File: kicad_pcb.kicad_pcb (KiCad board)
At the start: 2 copper layers, 285 x 95.1 mm, 163 parts, among them J1 USB_B_Mini, SW1 SW_Push, U1 ATmega32U4-AU, Y1 Resonator_Small

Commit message: rerouted the bottom row
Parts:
- added D23: D_Small, Diode_SMD:D_0805_2012Metric, B.Cu at (293.8, 120.0)
- added D38: D_Small, Diode_SMD:D_0805_2012Metric, B.Cu at (310.4, 120.0)
- added D66: D_Small, Diode_SMD:D_0805_2012Metric, B.Cu at (291.3, 120.0)
- added D69: D_Small, Diode_SMD:D_0805_2012Metric, B.Cu at (330.2, 120.0)
- added MX23: R ALT, MX_Alps_Hybrid:MX-2U-NoLED, F.Cu at (287.3, 125.4)
- added MX38: R WIN, MX_Alps_Hybrid:MX-1.25U-NoLED, F.Cu at (294.5, 125.4)
- added MX62-1: CTRL, MX_Alps_Hybrid:MX-1.5U-NoLED, F.Cu at (77.8, 125.4)
- added MX63-1: WIN, MX_Alps_Hybrid:MX-1.25U-NoLED, F.Cu at (104.0, 125.4)
- added MX64-1: ALT, MX_Alps_Hybrid:MX-1.5U-NoLED, F.Cu at (130.2, 125.4)
- added MX65-1: L SPACE, MX_Alps_Hybrid:MX-2.75U-ReversedStabilizers-NoLED, F.Cu at (170.7, 125.4)
- added MX66: R ALT, MX_Alps_Hybrid:MX-1.5U-NoLED, F.Cu at (268.3, 125.4)
- added MX69: R CTRL, MX_Alps_Hybrid:MX-2.25U-NoLED, F.Cu at (327.8, 125.4)
- added MX70-1: R SPACE, MX_Alps_Hybrid:MX-2.75U-NoLED, F.Cu at (242.1, 125.4)
- MX61: footprint MX_Alps_Hybrid:MXOnly-1U-NoLED -> MX_Alps_Hybrid:MX-1U-NoLED
- MX62, MX63, MX64: footprint MX_Alps_Hybrid:MXOnly-1.25U-NoLED -> MX_Alps_Hybrid:MX-1.25U-NoLED
- MX65: value LEFT SPACE -> L SPACE; footprint MX_Alps_Hybrid:MXOnly-2.25U-ReversedStabilizers-NoLED -> MX_Alps_Hybrid:MX-2.25U-ReversedStabilizers-NoLED
- MX70: value RIGHT SPACE -> R SPACE
- moved D70 26.7 mm to (262.7, 119.9), turned to 270 degrees
- moved D75 14.0 mm to (333.4, 120.0), turned to 270 degrees
- moved D71 10.9 mm to (269.9, 119.9), turned to 270 degrees
- moved D72 10.8 mm to (288.9, 120.0), turned to 270 degrees
- moved D74 10.8 mm to (327.0, 120.0), turned to 270 degrees
- moved D73 10.7 mm to (307.6, 120.0), turned to 270 degrees
- moved D61 4.62 mm to (81.0, 130.3)
- turned MX61 to 180 degrees
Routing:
- net COL7: track 82.1 -> 214.2 mm, vias 1 -> 2
- net COL8: track 90.6 -> 219.8 mm, vias 2 -> 4
- net COL5: track 93.4 -> 219.9 mm, vias 1 -> 3
- net ROW1: track 296.0 -> 352.8 mm, vias 4 -> 6
- net Net-(D66-Pad2): track 0.00 -> 34.6 mm
- net Net-(D23-Pad2): track 0.00 -> 34.2 mm
- net ROW2: track 286.1 -> 313.0 mm, vias 2 -> 4
- net Net-(D70-Pad2): track 9.31 -> 35.9 mm
- net Net-(D38-Pad2): track 0.00 -> 18.8 mm
- net Net-(D62-Pad2): track 9.31 -> 27.1 mm
- net COL9: track 133.1 -> 150.8 mm
- net COL1: track 189.1 -> 205.3 mm
- net Net-(D63-Pad2): track 9.31 -> 24.9 mm
- net Net-(D65-Pad2): track 9.31 -> 23.8 mm
- net Net-(D64-Pad2): track 9.37 -> 23.1 mm
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
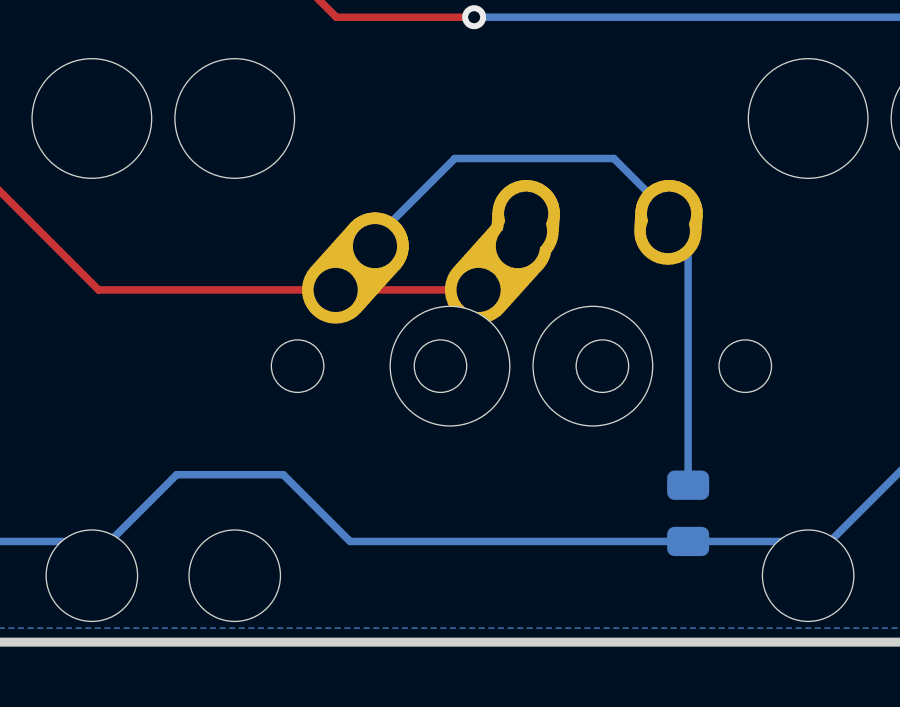
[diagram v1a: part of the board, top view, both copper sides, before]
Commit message: tidied up some overlapping pads
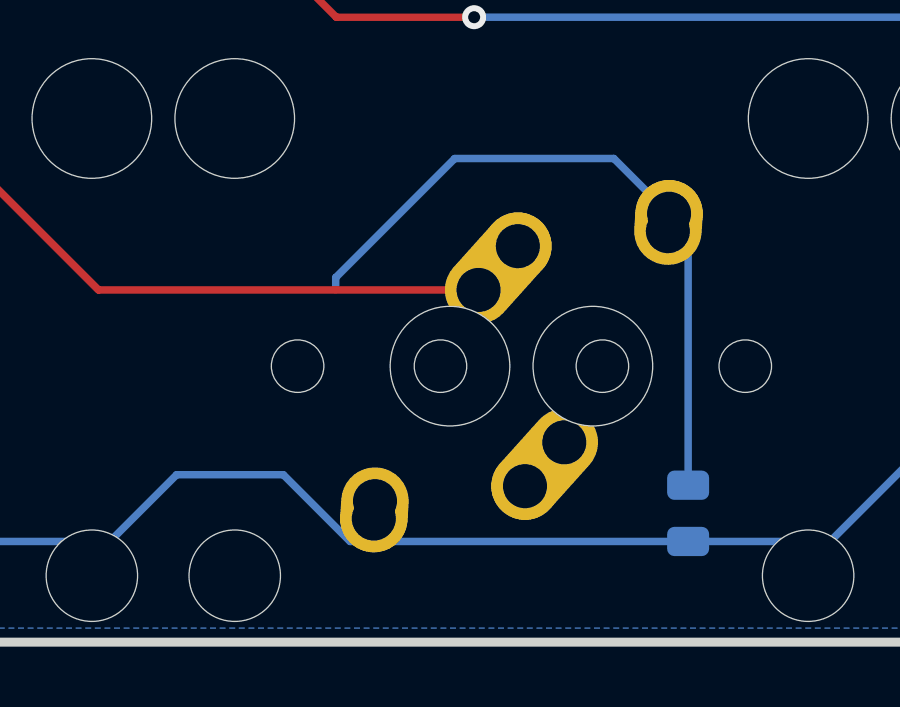
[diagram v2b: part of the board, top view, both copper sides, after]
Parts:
- MX65: value L SPACE -> L SPACE (2.25u)
- MX65-1: value L SPACE -> L SPACE (2.75u); footprint MX_Alps_Hybrid:MX-2.75U-ReversedStabilizers-NoLED -> MX_Alps_Hybrid:MX-2.75U-NoLED
- turned MX65-1 to 180 degrees
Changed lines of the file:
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@@
       (effects (font (size 1 1) (thickness 0.15)))
     )
-    (fp_text value "L SPACE" (at 0 -7.9375) (layer Dwgs.User)
+    (fp_text value "L SPACE (2.25u)" (at -2.38125 -7.9375) (layer Dwgs.User)
       (effects (font (size 1 1) (thickness 0.15)))
     )
@@
     (pad 2 thru_hole oval (at 2.5 -4.5 86.0548) (size 2.831378 2.25) (drill 1.47 (offset 0.290689 0)) (layers *.Cu B.Mask)
       (net 87 "Net-(D64-Pad2)"))
-  )
-  (module MX_Alps_Hybrid:MX-2.75U-ReversedStabilizers-NoLED (layer F.Cu)
-    (at 170.65625 125.4125)
-    (fp_text reference MX65-1 (at 0 3.175) (layer Dwgs.User)
-      (effects (font (size 1 1) (thickness 0.15)))
-    )
-    (fp_text value "L SPACE" (at 0 -7.9375) (layer Dwgs.User)
-      (effects (font (size 1 1) (thickness 0.15)))
-    )
-    (fp_line (start 5 -7) (end 7 -7) (layer Dwgs.User) (width 0.15))
-    (fp_line (start 7 -7) (end 7 -5) (layer Dwgs.User) (width 0.15))
-    (fp_line (start 5 7) (end 7 7) (layer Dwgs.User) (width 0.15))
-    (fp_line (start 7 7) (end 7 5) (layer Dwgs.User) (width 0.15))
-    (fp_line (start -7 5) (end -7 7) (layer Dwgs.User) (width 0.15))
-    (fp_line (start -7 7) (end -5 7) (layer Dwgs.User) (width 0.15))
-    (fp_line (start -5 -7) (end -7 -7) (layer Dwgs.User) (width 0.15))
-    (fp_line (start -7 -7) (end -7 -5) (layer Dwgs.User) (width 0.15))
-    (fp_line (start -26.19375 -9.525) (end 26.19375 -9.525) (layer Dwgs.User) (width 0.15))
-    (fp_line (start 26.19375 -9.525) (end 26.19375 9.525) (layer Dwgs.User) (width 0.15))
-    (fp_line (start -26.19375 9.525) (end 26.19375 9.525) (layer Dwgs.User) (width 0.15))
-    (fp_line (start -26.19375 9.525) (end -26.19375 -9.525) (layer Dwgs.User) (width 0.15))
-    (pad 2 thru_hole oval (at 2.5 -4.5 86.0548) (size 2.831378 2.25) (drill 1.47 (offset 0.290689 0)) (layers *.Cu B.Mask)
-      (net 22 COL4))
-    (pad 2 thru_hole circle (at 2.54 -5.08) (size 2.25 2.25) (drill 1.47) (layers *.Cu B.Mask)
-      (net 22 COL4))
-    (pad 1 thru_hole oval (at -3.81 -2.54 48.0996) (size 4.211556 2.25) (drill 1.47 (offset 0.980778 0)) (layers *.Cu B.Mask)
-      (net 88 "Net-(D65-Pad2)"))
-    (pad "" np_thru_hole circle (at 0 0) (size 3.9878 3.9878) (drill 3.9878) (layers *.Cu *.Mask))
-    (pad 1 thru_hole circle (at -2.5 -4) (size 2.25 2.25) (drill 1.47) (layers *.Cu B.Mask)
-      (net 88 "Net-(D65-Pad2)"))
-    (pad "" np_thru_hole circle (at -5.08 0 48.0996) (size 1.75 1.75) (drill 1.75) (layers *.Cu *.Mask))
-    (pad "" np_thru_hole circle (at 5.08 0 48.0996) (size 1.75 1.75) (drill 1.75) (layers *.Cu *.Mask))
-    (pad "" np_thru_hole circle (at -11.938 6.985) (size 3.048 3.048) (drill 3.048) (layers *.Cu *.Mask))
-    (pad "" np_thru_hole circle (at 11.938 6.985) (size 3.048 3.048) (drill 3.048) (layers *.Cu *.Mask))
-    (pad "" np_thru_hole circle (at -11.938 -8.255) (size 3.9878 3.9878) (drill 3.9878) (layers *.Cu *.Mask))
-    (pad "" np_thru_hole circle (at 11.938 -8.255) (size 3.9878 3.9878) (drill 3.9878) (layers *.Cu *.Mask))
   )
   (module Diode_SMD:D_0805_2012Metric (layer B.Cu)
@@
     )
   )
+  (module MX_Alps_Hybrid:MX-2.75U-NoLED (layer F.Cu)
+    (at 170.65625 125.4125 180)
+    (fp_text reference MX65-1 (at 0 3.175) (layer Dwgs.User)
+      (effects (font (size 1 1) (thickness 0.15)))
+    )
+    (fp_text value "L SPACE (2.75u)" (at -2.38125 -7.9375) (layer Dwgs.User)
+      (effects (font (size 1 1) (thickness 0.15)))
+    )
+    (fp_line (start 5 -7) (end 7 -7) (layer Dwgs.User) (width 0.15))
+    (fp_line (start 7 -7) (end 7 -5) (layer Dwgs.User) (width 0.15))
+    (fp_line (start 5 7) (end 7 7) (layer Dwgs.User) (width 0.15))
+    (fp_line (start 7 7) (end 7 5) (layer Dwgs.User) (width 0.15))
+    (fp_line (start -7 5) (end -7 7) (layer Dwgs.User) (width 0.15))
+    (fp_line (start -7 7) (end -5 7) (layer Dwgs.User) (width 0.15))
+    (fp_line (start -5 -7) (end -7 -7) (layer Dwgs.User) (width 0.15))
+    (fp_line (start -7 -7) (end -7 -5) (layer Dwgs.User) (width 0.15))
+    (fp_line (start -26.19375 -9.525) (end 26.19375 -9.525) (layer Dwgs.User) (width 0.15))
+    (fp_line (start 26.19375 -9.525) (end 26.19375 9.525) (layer Dwgs.User) (width 0.15))
+    (fp_line (start -26.19375 9.525) (end 26.19375 9.525) (layer Dwgs.User) (width 0.15))
+    (fp_line (start -26.19375 9.525) (end -26.19375 -9.525) (layer Dwgs.User) (width 0.15))
+    (pad 2 thru_hole oval (at 2.5 -4.5 266.0548) (size 2.831378 2.25) (drill 1.47 (offset 0.290689 0)) (layers *.Cu B.Mask)
+      (net 22 COL4))
+    (pad 2 thru_hole circle (at 2.54 -5.08 180) (size 2.25 2.25) (drill 1.47) (layers *.Cu B.Mask)
+      (net 22 COL4))
+    (pad 1 thru_hole oval (at -3.81 -2.54 228.0996) (size 4.211556 2.25) (drill 1.47 (offset 0.980778 0)) (layers *.Cu B.Mask)
+      (net 88 "Net-(D65-Pad2)"))
+    (pad "" np_thru_hole circle (at 0 0 180) (size 3.9878 3.9878) (drill 3.9878) (layers *.Cu *.Mask))
+    (pad 1 thru_hole circle (at -2.5 -4 180) (size 2.25 2.25) (drill 1.47) (layers *.Cu B.Mask)
+      (net 88 "Net-(D65-Pad2)"))
+    (pad "" np_thru_hole circle (at -5.08 0 228.0996) (size 1.75 1.75) (drill 1.75) (layers *.Cu *.Mask))
+    (pad "" np_thru_hole circle (at 5.08 0 228.0996) (size 1.75 1.75) (drill 1.75) (layers *.Cu *.Mask))
+    (pad "" np_thru_hole circle (at -11.938 -6.985 180) (size 3.048 3.048) (drill 3.048) (layers *.Cu *.Mask))
+    (pad "" np_thru_hole circle (at 11.938 -6.985 180) (size 3.048 3.048) (drill 3.048) (layers *.Cu *.Mask))
+    (pad "" np_thru_hole circle (at -11.938 8.255 180) (size 3.9878 3.9878) (drill 3.9878) (layers *.Cu *.Mask))
+    (pad "" np_thru_hole circle (at 11.938 8.255 180) (size 3.9878 3.9878) (drill 3.9878) (layers *.Cu *.Mask))
+  )
   (gr_text "Katana60 revision 2\nby RominRonin in association with CandyKeys.com" (at 182.5625 96.8375) (layer B.SilkS)

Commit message: Introduced mx and alps footprints for every switch
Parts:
- removed MX89: ALT-BACKSPACE, MX_Alps_Hybrid:MXOnly-2U-NoLED
- added MX30-2: BACKSPACE (2u), MX_Alps_Hybrid:MX-2U-NoLED, F.Cu at (330.2, 49.2)
- MX1, MX10, MX11, MX12, MX13, MX14, MX15, MX17, MX18, MX19, MX2, MX20, MX21, MX22, MX24, MX25, MX26, MX27, MX28, MX29, MX3, MX31, MX32, MX33, MX34, MX35, MX36, MX37, MX39, MX4, MX40, MX41, MX42, MX43, MX44, MX45, MX46, MX47, MX48, MX49, MX5, MX50, MX51, MX52, MX53, MX54, MX55, MX56, MX57, MX58, MX59, MX6, MX60, MX68, MX7, MX71, MX72, MX73, MX74, MX75, MX8, MX9: footprint MX_Alps_Hybrid:MXOnly-1U-NoLED -> MX_Alps_Hybrid:MX-1U-NoLED
- MX16: value TAB_orth -> TAB; footprint MX_Alps_Hybrid:MXOnly-1U-NoLED -> MX_Alps_Hybrid:MX-1.5U-NoLED
- MX16-1: value TAB -> TAB_orth; footprint MX_Alps_Hybrid:MXOnly-1.5U-NoLED -> MX_Alps_Hybrid:MX-1U-NoLED
- MX30: value BACKSPACE_orth -> BACKSPACE; footprint MX_Alps_Hybrid:MXOnly-1U-NoLED -> MX_Alps_Hybrid:MX-1.5U-NoLED
- MX30-1: value BACKSPACE -> BACKSPACE_orth; footprint MX_Alps_Hybrid:MXOnly-1.5U-NoLED -> MX_Alps_Hybrid:MX-1U-NoLED
- MX31-1, MX37-1, MX39-1, MX45-1: footprint MX_Alps_Hybrid:MXOnly-1.25U-NoLED -> MX_Alps_Hybrid:MX-1.25U-NoLED
- MX70: footprint MX_Alps_Hybrid:MXOnly-2U-ReversedStabilizers-NoLED -> MX_Alps_Hybrid:MX-2U-ReversedStabilizers-NoLED
- moved MX16 4.76 mm to (77.8, 68.3)
- moved MX16-1 4.76 mm to (82.5, 68.3)
- moved MX30 4.76 mm to (335.0, 68.3)
- moved MX30-1 4.76 mm to (330.2, 68.3)
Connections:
- MX16 pad 1: COL0 -> Net-(D16-Pad2)
- MX16 pad 2: Net-(D16-Pad2) -> COL0
- MX30-1 pad 1: COL14 -> Net-(D30-Pad2)
- MX30-1 pad 2: Net-(D30-Pad2) -> COL14
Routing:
- net COL0: track 230.3 -> 242.0 mm
- net Net-(D16-Pad2): track 27.7 -> 36.6 mm
- net COL4: track 149.6 -> 158.3 mm
- net Net-(D65-Pad2): track 23.8 -> 15.4 mm
- net Net-(D30-Pad2): track 34.8 -> 40.7 mm
- net ROW4: track 326.8 -> 328.2 mm, vias 2 -> 3
- net COL14: track 242.9 -> 242.0 mm
- net Net-(R2-Pad1): track 137.4 -> 136.9 mm
- net +5V: track 348.8 -> 349.2 mm, vias 10 -> 9
- net ROW0: track 316.6 -> 316.7 mm, vias 0 -> 2
- net ROW3: vias 0 -> 2

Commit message: Added symmetric 7u bottom row
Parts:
- added MX38-2: R WIN (1u), MX_Alps_Hybrid:MX-1U-NoLED, F.Cu at (311.1, 125.4)
- added MX6-2: CENTER (7u), MX_Alps_Hybrid:MX-7U-ReversedStabilizers-NoLED, F.Cu at (206.4, 125.4)
- added MX63-2: WIN (1u), MX_Alps_Hybrid:MX-1U-NoLED, F.Cu at (101.6, 125.4)
- added MX64-2: ALT (1.5u), MX_Alps_Hybrid:MX-1.5U-NoLED, F.Cu at (125.4, 125.4)
- added MX69-2: R CTRL (1.5u), MX_Alps_Hybrid:MX-1.5U-NoLED, F.Cu at (335.0, 125.4)
- moved D70 24.6 mm to (238.3, 117.2), turned to 180 degrees
- moved D63 4.76 mm to (116.7, 130.3)
- moved D62 2.38 mm to (95.2, 130.3)
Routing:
- net Net-(D69-Pad2): track 13.5 -> 60.0 mm, vias 0 -> 2
- net COL2: track 183.0 -> 207.6 mm
- net Net-(D64-Pad2): track 23.1 -> 46.1 mm, vias 0 -> 2
- net Net-(D63-Pad2): track 24.9 -> 46.6 mm
- net Net-(D70-Pad2): track 35.9 -> 14.3 mm
- net COL3: track 167.5 -> 187.4 mm
- net ROW1: track 352.8 -> 361.9 mm
- net Net-(D62-Pad2): track 27.1 -> 33.1 mm
- net COL8: track 219.8 -> 225.5 mm
- net COL7: track 214.2 -> 218.9 mm
- net ROW4: track 328.2 -> 332.2 mm, vias 3 -> 7
- net Net-(D38-Pad2): track 18.8 -> 22.0 mm
- net Net-(D23-Pad2): track 34.2 -> 36.8 mm
- net Net-(D66-Pad2): track 34.6 -> 37.1 mm
- net Net-(D75-Pad2): track 9.14 -> 11.0 mm
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
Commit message: improved tracing
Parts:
- moved D16 5.56 mm to (80.2, 72.9)
- moved D66 0.64 mm to (290.7, 120.0)
- moved D23 0.63 mm to (293.1, 120.0)
- moved D72 0.63 mm to (288.3, 120.0)
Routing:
- net Net-(D69-Pad2): track 60.0 -> 35.9 mm, vias 2 -> 0
- net Net-(D30-Pad2): track 40.7 -> 57.9 mm, vias 0 -> 1
- net Net-(D16-Pad2): track 36.6 -> 48.8 mm, vias 0 -> 2
- net Net-(D63-Pad2): track 46.6 -> 55.1 mm
- net ROW1: track 361.9 -> 368.0 mm
- net Net-(D45-Pad2): track 21.8 -> 27.6 mm
- net Net-(D22-Pad2): track 22.2 -> 20.0 mm
- net Net-(D66-Pad2): track 37.1 -> 39.1 mm, vias 0 -> 2
- net Net-(D23-Pad2): track 36.8 -> 35.8 mm
- net ROW4: track 332.2 -> 331.5 mm

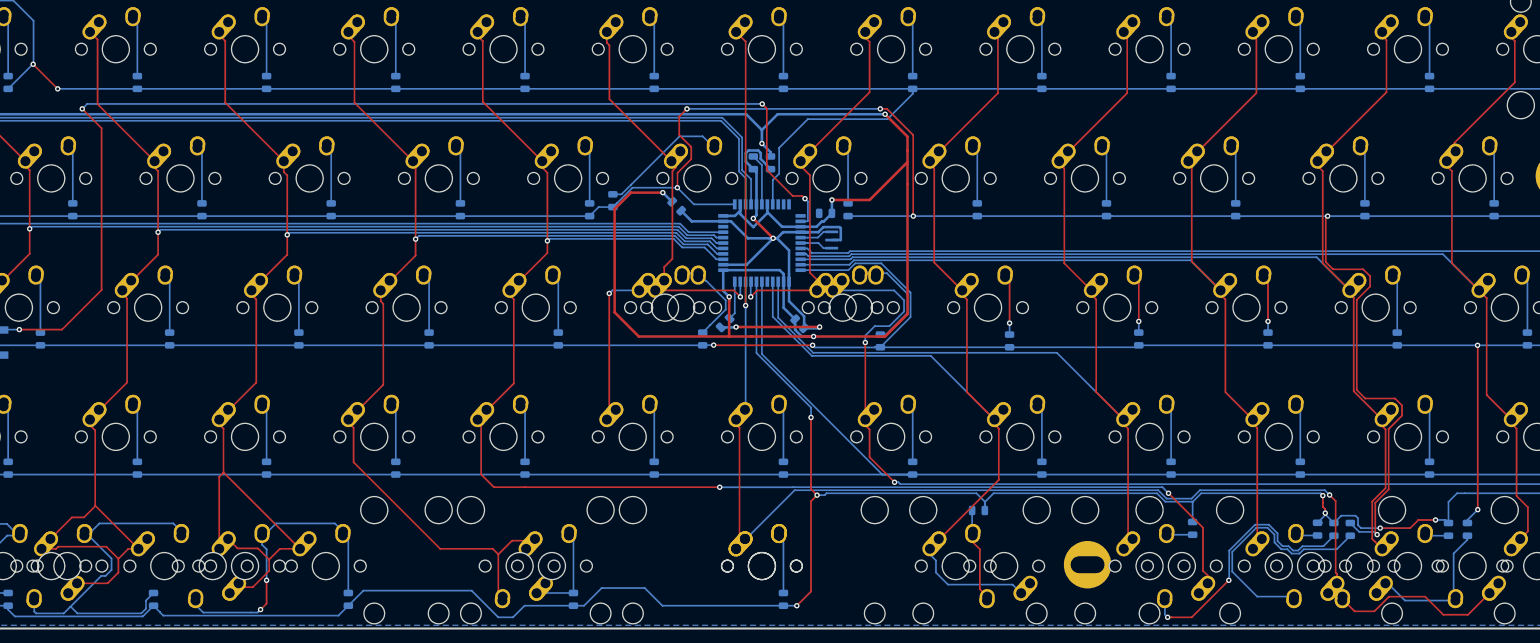
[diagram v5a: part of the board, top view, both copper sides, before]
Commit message: created additional space around the stabilisers to prevent shorting
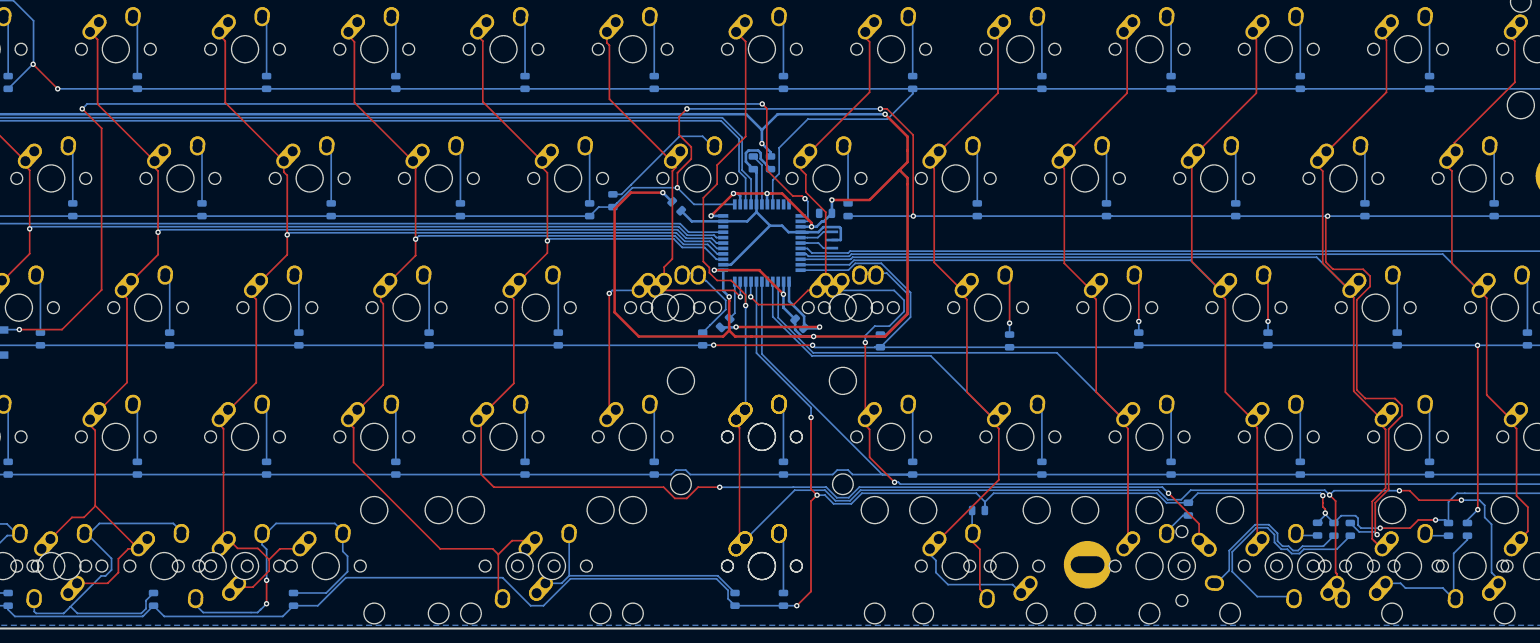
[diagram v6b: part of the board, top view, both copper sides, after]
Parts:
- added MX53-1: DELETE, MX_Alps_Hybrid:MX-2.75U-ReversedStabilizers-NoLED, F.Cu at (206.4, 106.4)
- moved G*** 95.1 mm to (293.5, 58.7)
- moved D65 23.8 mm to (202.4, 130.3)
- moved D64 8.08 mm to (137.3, 130.3)
- moved D71 2.91 mm to (269.2, 117.0)
- turned MX66 to 270 degrees
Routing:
- net Net-(D65-Pad2): track 15.4 -> 37.5 mm
- net COL7: track 218.9 -> 237.3 mm, vias 2 -> 4
- net COL3: track 187.4 -> 170.0 mm
- net Net-(D66-Pad2): track 39.1 -> 26.3 mm, vias 2 -> 0
- net COL2: track 207.6 -> 195.4 mm
- net GND: track 98.0 -> 86.3 mm, vias 6 -> 4
- net +5V: track 349.2 -> 358.5 mm, vias 9 -> 15
- net Net-(D64-Pad2): track 46.1 -> 52.7 mm
- net COL5: track 219.9 -> 215.8 mm
- net Net-(D71-Pad2): track 4.00 -> 5.41 mm
- net ROW3: track 307.0 -> 308.1 mm
- net COL8: track 225.5 -> 226.2 mm
- net Net-(D38-Pad2): track 22.0 -> 22.7 mm
